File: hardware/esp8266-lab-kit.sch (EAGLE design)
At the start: 13 parts, among them CON1 M025MM, U1 NODEMCU_DEVKIT_V1.0, U2 DHT11, U3 HC-SR501

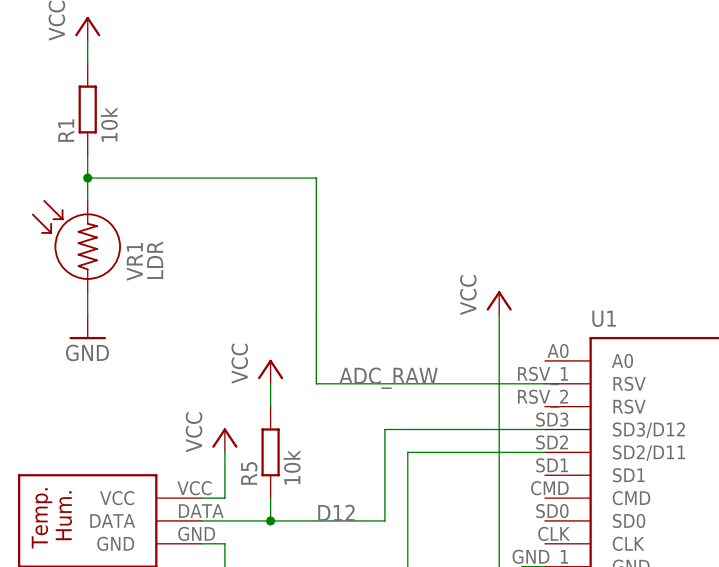
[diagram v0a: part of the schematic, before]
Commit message: Update ELK to Revision B, fixing the ADC kerfuffle.
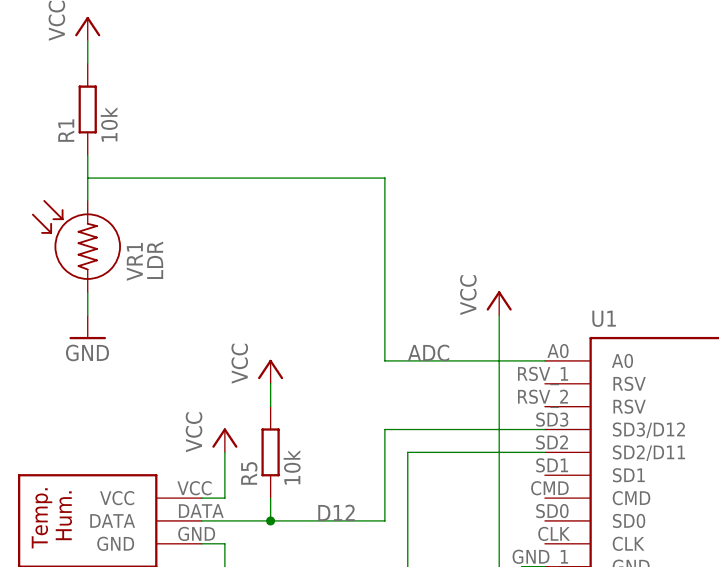
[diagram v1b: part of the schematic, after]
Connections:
- removed net ADC_RAW: R1.1, U1.RSV@1, VR1.2
- new net ADC: R1.1, U1.A0, VR1.2
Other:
- note added: "Revision B"
- note removed: "Revision A"
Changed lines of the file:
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@@
 <?xml version="1.0" encoding="utf-8"?>
 <!DOCTYPE eagle SYSTEM "eagle.dtd">
-<eagle version="7.3.0">
+<eagle version="7.5.0">
 <drawing>
 <settings>
@@
 <text x="181.61" y="27.94" size="1.524" layer="97" font="vector" rot="R90">As part of the
 NodeMCU board</text>
-<text x="210.82" y="11.43" size="1.778" layer="203" distance="60">Revision A</text>
+<text x="210.82" y="11.43" size="1.778" layer="203" distance="60">Revision B</text>
 </plain>
 <instances>
@@
 </segment>
 </net>
-<net name="ADC_RAW" class="0">
-<segment>
-<pinref part="VR1" gate="G$1" pin="2"/>
-<pinref part="R1" gate="G$1" pin="1"/>
-<wire x1="53.34" y1="149.86" x2="53.34" y2="147.32" width="0.1524" layer="91"/>
-<wire x1="53.34" y1="147.32" x2="53.34" y2="144.78" width="0.1524" layer="91"/>
-<wire x1="53.34" y1="147.32" x2="78.74" y2="147.32" width="0.1524" layer="91"/>
-<wire x1="78.74" y1="147.32" x2="78.74" y2="132.08" width="0.1524" layer="91"/>
-<junction x="53.34" y="147.32"/>
-<pinref part="U1" gate="G$1" pin="RSV@1"/>
-<wire x1="104.14" y1="124.46" x2="78.74" y2="124.46" width="0.1524" layer="91"/>
-<wire x1="78.74" y1="124.46" x2="78.74" y2="132.08" width="0.1524" layer="91"/>
-<label x="81.28" y="124.46" size="1.778" layer="95"/>
-</segment>
-</net>
 <net name="VCC" class="0">
 <segment>
@@
 </segment>
 </net>
+<net name="ADC" class="0">
+<segment>
+<pinref part="VR1" gate="G$1" pin="2"/>
+<pinref part="R1" gate="G$1" pin="1"/>
+<wire x1="53.34" y1="149.86" x2="53.34" y2="147.32" width="0.1524" layer="91"/>
+<wire x1="53.34" y1="147.32" x2="53.34" y2="144.78" width="0.1524" layer="91"/>
+<pinref part="U1" gate="G$1" pin="A0"/>
+<wire x1="104.14" y1="127" x2="86.36" y2="127" width="0.1524" layer="91"/>
+<wire x1="86.36" y1="127" x2="86.36" y2="147.32" width="0.1524" layer="91"/>
+<wire x1="86.36" y1="147.32" x2="53.34" y2="147.32" width="0.1524" layer="91"/>
+<label x="88.9" y="127" size="1.778" layer="95"/>
+</segment>
+</net>
